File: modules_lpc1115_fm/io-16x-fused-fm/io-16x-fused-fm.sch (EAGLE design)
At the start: 144 parts, among them IC5 LPC1115, IC6 ATAES132A-SHEQ-T, J1 62000611622, J2 1771017, J3 1770953, Q3 ASFL, U3 EEPROM, X1 MICROMATCH-10SMD

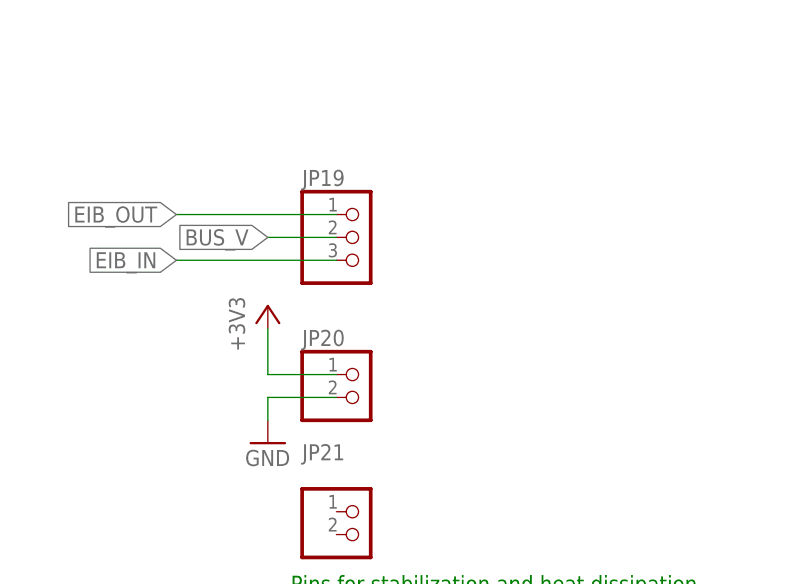
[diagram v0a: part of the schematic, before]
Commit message: [IO16xFM] - new branch for designing a slightly smaller BRD
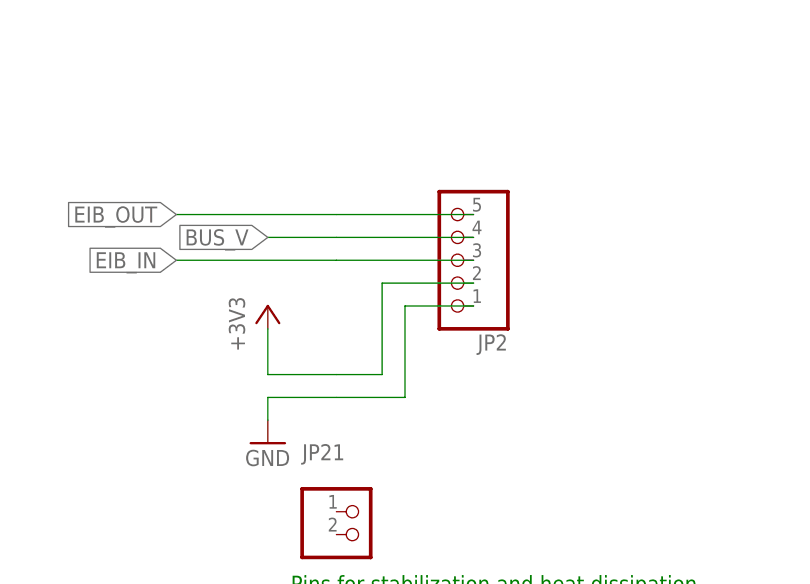
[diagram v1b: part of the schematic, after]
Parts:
- removed JP19: (no value), pinhead_dmx:PINHD-1X3
- removed JP20: (no value), pinhead_dmx:PINHD-1X2
- added JP2: (no value), pinhead_dmx:PINHD-1X5
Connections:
- net +3V3: now also JP2.2; no longer JP20.1
- net BUS_V: now also JP2.4; no longer JP19.2
- net EIB_IN: now also JP2.3; no longer JP19.3
- net EIB_OUT: now also JP2.5; no longer JP19.1
- net GND: now also JP2.1; no longer JP20.2
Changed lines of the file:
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@@
 <part name="R69" library="rcl" library_urn="urn:adsk.eagle:library:334" deviceset="R-EU_" device="R0805" package3d_urn="urn:adsk.eagle:package:23553/2" value="1k"/>
 <part name="GND66" library="supply1" library_urn="urn:adsk.eagle:library:371" deviceset="GND" device=""/>
-<part name="JP19" library="pinhead_dmx" deviceset="PINHD-1X3" device="" package3d_urn="urn:adsk.eagle:package:22458/2"/>
 <part name="C34" library="rcl" library_urn="urn:adsk.eagle:library:334" deviceset="C-EU" device="C0805" package3d_urn="urn:adsk.eagle:package:23617/2" value="100nF"/>
 <part name="FB17" library="RCL_for_Selfbus-Projects" deviceset="FERRITE2" device="_0805MP" package3d_urn="urn:adsk.eagle:package:41867834/2" value="1.5kΩ@100MHz"/>
@@
 <part name="FB23" library="RCL_for_Selfbus-Projects" deviceset="FERRITE2" device="_0805MP" package3d_urn="urn:adsk.eagle:package:41867834/2" value="1.5kΩ@100MHz"/>
 <part name="FB24" library="RCL_for_Selfbus-Projects" deviceset="FERRITE2" device="_0805MP" package3d_urn="urn:adsk.eagle:package:41867834/2" value="1.5kΩ@100MHz"/>
-<part name="JP20" library="pinhead_dmx" deviceset="PINHD-1X2" device="" package3d_urn="urn:adsk.eagle:package:22435/2"/>
 <part name="JP21" library="pinhead_dmx" deviceset="PINHD-1X2" device="" package3d_urn="urn:adsk.eagle:package:22435/2"/>
 <part name="R70" library="rcl" library_urn="urn:adsk.eagle:library:334" deviceset="R-EU_" device="R0805" package3d_urn="urn:adsk.eagle:package:23553/2" value="3,3k"/>
@@
 <part name="TP5" library="testpad" library_urn="urn:adsk.eagle:library:385" deviceset="TPSQ" device="TP08R" package3d_urn="urn:adsk.eagle:package:27956/1"/>
 <part name="TP6" library="testpad" library_urn="urn:adsk.eagle:library:385" deviceset="TPSQ" device="TP08R" package3d_urn="urn:adsk.eagle:package:27956/1"/>
+<part name="JP2" library="pinhead_dmx" deviceset="PINHD-1X5" device="" package3d_urn="urn:adsk.eagle:package:22469/2"/>
 </parts>
 <sheets>
@@
 <attribute name="VALUE" x="391.16" y="269.24" size="1.778" layer="96"/>
 </instance>
-<instance part="JP19" gate="A" x="403.86" y="294.64" smashed="yes">
-<attribute name="NAME" x="397.51" y="300.355" size="1.778" layer="95"/>
-<attribute name="VALUE" x="397.51" y="287.02" size="1.778" layer="96"/>
-</instance>
 <instance part="C34" gate="G$1" x="251.46" y="22.86" smashed="yes" rot="R180">
 <attribute name="NAME" x="250.952" y="21.971" size="1.778" layer="95" rot="R180"/>
@@
 <attribute name="VALUE" x="80.01" y="285.115" size="1.27" layer="95" rot="R180"/>
 </instance>
-<instance part="JP20" gate="G$1" x="403.86" y="276.86" smashed="yes">
-<attribute name="NAME" x="397.51" y="282.575" size="1.778" layer="95"/>
-<attribute name="VALUE" x="397.51" y="271.78" size="1.778" layer="96"/>
-</instance>
 <instance part="JP21" gate="G$1" x="403.86" y="261.62" smashed="yes">
 <attribute name="NAME" x="397.51" y="269.875" size="1.778" layer="95"/>
@@
 <attribute name="NAME" x="104.775" y="40.64" size="1.778" layer="95" rot="R270"/>
 <attribute name="TP_SIGNAL_NAME" x="107.95" y="35.56" size="1.778" layer="97" rot="R270"/>
+</instance>
+<instance part="JP2" gate="A" x="414.02" y="292.1" smashed="yes" rot="R180">
+<attribute name="NAME" x="420.37" y="283.845" size="1.778" layer="95" rot="R180"/>
+<attribute name="VALUE" x="420.37" y="302.26" size="1.778" layer="96" rot="R180"/>
 </instance>
 </instances>
@@
 <segment>
 <pinref part="GND66" gate="1" pin="GND"/>
-<pinref part="JP20" gate="G$1" pin="2"/>
 <wire x1="401.32" y1="276.86" x2="393.7" y2="276.86" width="0.1524" layer="91"/>
 <wire x1="393.7" y1="276.86" x2="393.7" y2="274.32" width="0.1524" layer="91"/>
+<wire x1="401.32" y1="276.86" x2="408.94" y2="276.86" width="0.1524" layer="91"/>
+<wire x1="408.94" y1="276.86" x2="408.94" y2="287.02" width="0.1524" layer="91"/>
+<pinref part="JP2" gate="A" pin="1"/>
+<wire x1="408.94" y1="287.02" x2="416.56" y2="287.02" width="0.1524" layer="91"/>
 </segment>
 <segment>
@@
 <net name="EIB_OUT" class="0">
 <segment>
-<pinref part="JP19" gate="A" pin="1"/>
 <wire x1="401.32" y1="297.18" x2="383.54" y2="297.18" width="0.1524" layer="91"/>
 <label x="383.54" y="297.18" size="1.778" layer="95" rot="R180" xref="yes"/>
+<pinref part="JP2" gate="A" pin="5"/>
+<wire x1="401.32" y1="297.18" x2="416.56" y2="297.18" width="0.1524" layer="91"/>
 </segment>
 <segment>
@@
 </segment>
 <segment>
-<pinref part="JP19" gate="A" pin="2"/>
 <wire x1="401.32" y1="294.64" x2="393.7" y2="294.64" width="0.1524" layer="91"/>
 <label x="393.7" y="294.64" size="1.778" layer="95" rot="R180" xref="yes"/>
+<pinref part="JP2" gate="A" pin="4"/>
+<wire x1="401.32" y1="294.64" x2="416.56" y2="294.64" width="0.1524" layer="91"/>
 </segment>
 </net>
@@
 </segment>
 <segment>
-<pinref part="JP20" gate="G$1" pin="1"/>
 <wire x1="393.7" y1="279.4" x2="401.32" y2="279.4" width="0.1524" layer="91"/>
 <pinref part="P+40" gate="G$1" pin="+3V3"/>
 <wire x1="393.7" y1="284.48" x2="393.7" y2="279.4" width="0.1524" layer="91"/>
+<pinref part="JP2" gate="A" pin="2"/>
+<wire x1="406.4" y1="289.56" x2="416.56" y2="289.56" width="0.1524" layer="91"/>
+<wire x1="401.32" y1="279.4" x2="406.4" y2="279.4" width="0.1524" layer="91"/>
+<wire x1="406.4" y1="279.4" x2="406.4" y2="289.56" width="0.1524" layer="91"/>
 </segment>
 <segment>
@@
 <net name="EIB_IN" class="0">
 <segment>
-<pinref part="JP19" gate="A" pin="3"/>
 <wire x1="401.32" y1="292.1" x2="383.54" y2="292.1" width="0.1524" layer="91"/>
 <label x="383.54" y="292.1" size="1.778" layer="95" rot="R180" xref="yes"/>
-</segment>
-<segment>
+<pinref part="JP2" gate="A" pin="3"/>
+<wire x1="401.32" y1="292.1" x2="416.56" y2="292.1" width="0.1524" layer="91"/>
+</segment>
+<segment>

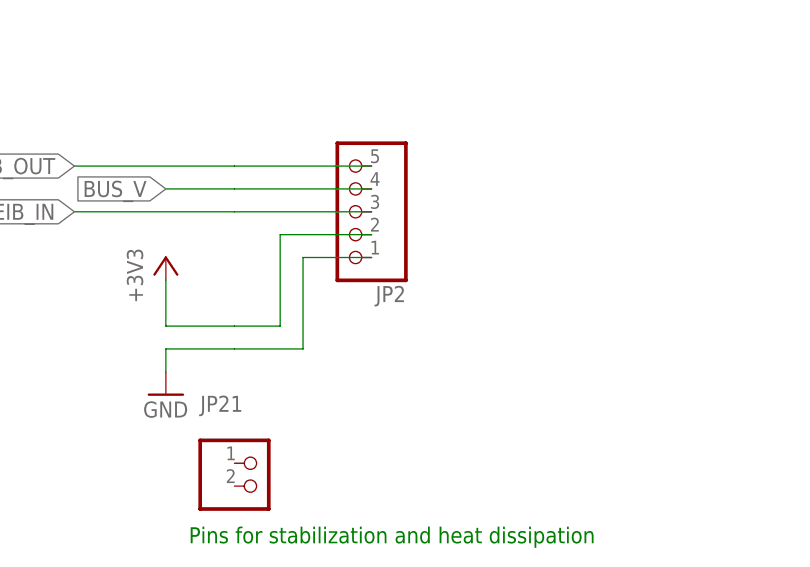
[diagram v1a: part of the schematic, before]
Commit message: [IO16xFM] - rearranged I2C and SPI connectors
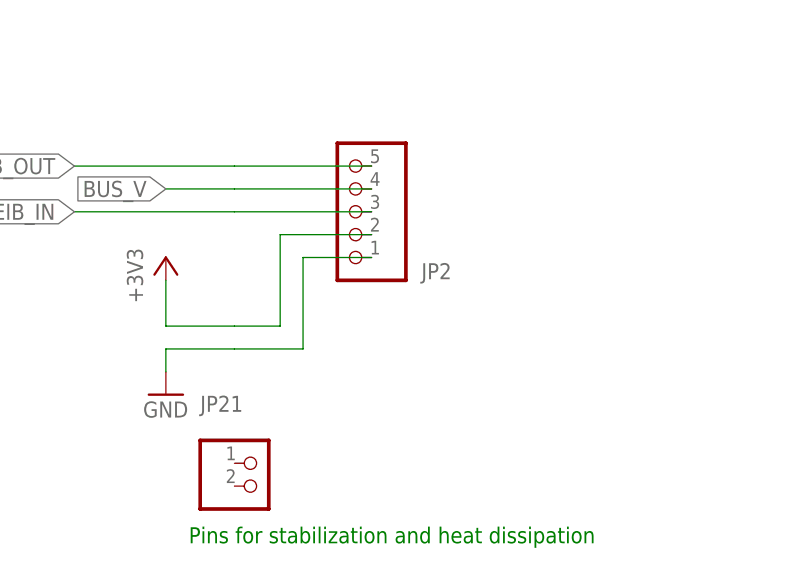
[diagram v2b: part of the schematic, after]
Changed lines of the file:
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@@
 </instance>
 <instance part="JP2" gate="A" x="414.02" y="292.1" smashed="yes" rot="R180">
-<attribute name="NAME" x="420.37" y="283.845" size="1.778" layer="95" rot="R180"/>
+<attribute name="NAME" x="425.45" y="286.385" size="1.778" layer="95" rot="R180"/>
 <attribute name="VALUE" x="420.37" y="302.26" size="1.778" layer="96" rot="R180"/>
 </instance>
